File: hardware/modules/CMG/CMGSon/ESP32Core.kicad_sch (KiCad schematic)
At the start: 22 parts, among them SW1 RESET_sw, U1 TPS3820, U2 SN65HVD230, U3 ESP32-S3-WROOM-1

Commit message: 一旦回路図完成
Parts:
- renumbered C3 to C201, C4 to C202, C1 to C203, C2 to C204, D1 to D201, D2 to D202, D3 to D203, D5 to D204, D6 to D205, D4 to D206, R1 to R201, R2 to R202, R5 to R203, R4 to R204, R6 to R205, R3 to R206, R7 to R207, SW1 to SW201, U3 to U201, U1 to U202, U2 to U203, USB1 to USB201
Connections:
- net VUSB renamed VBUS
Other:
- note removed: "CC pin 56kΩ for 0.5A 22kΩ for 1.5A 10kΩ for 3.0A"

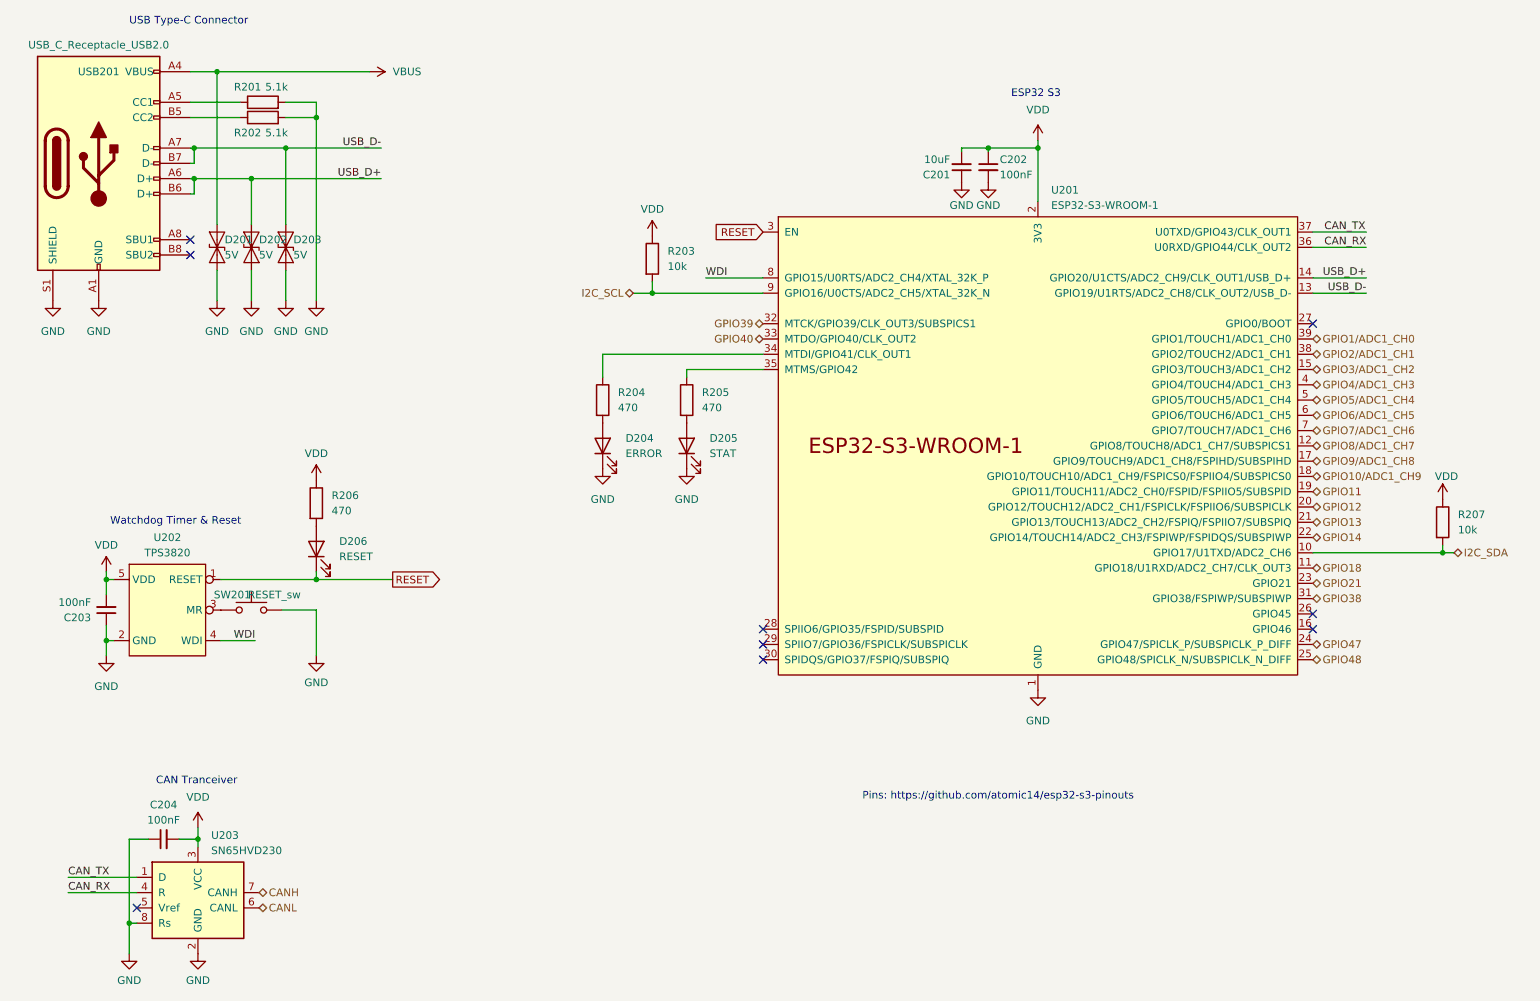
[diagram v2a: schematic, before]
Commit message: Sonも修正
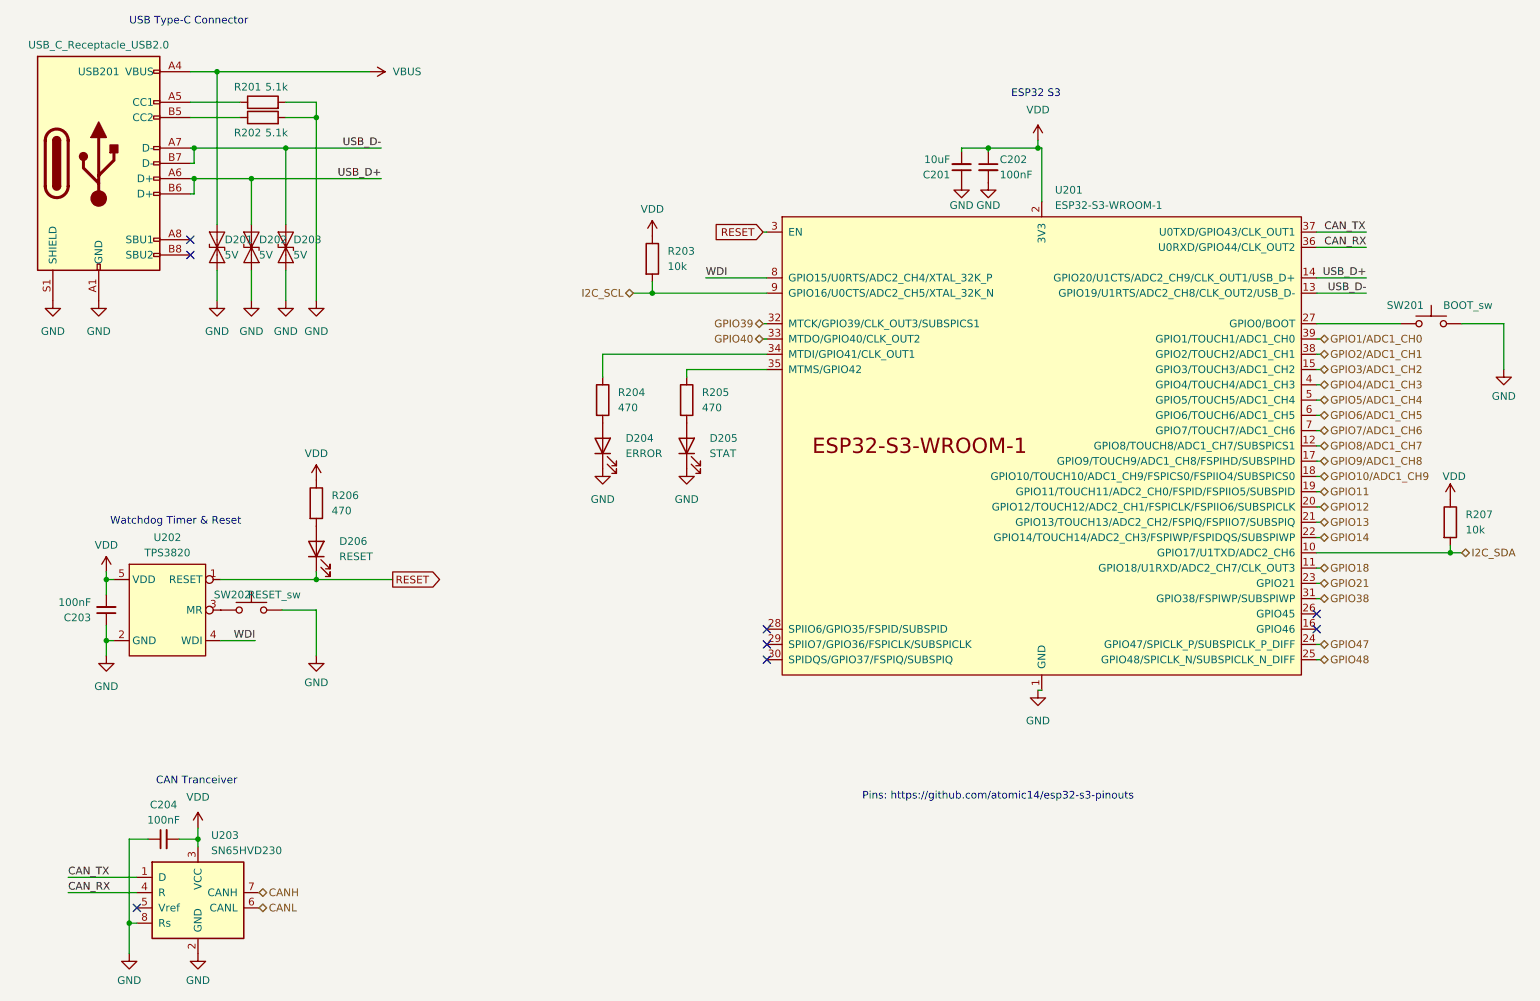
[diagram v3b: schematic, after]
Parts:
- added SW201: BOOT_sw, WOBCLibrary:TVAF06-A020B-R, symbol Switch:SW_Push
- USB201: LCSC C2856766 -> C720625
- renumbered SW201 to SW202
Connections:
- net GND: now also SW201.2
- net at U201.27 (GPIO0/BOOT): now also SW201.1
- no-connect marks 9 -> 8
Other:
- moved on the sheet: R207, U201
